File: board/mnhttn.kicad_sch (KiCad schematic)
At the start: 10 parts, among them SW1 SW_Push, SW2 SW_SPDT, SW3 SW_Push, SW4 SW_SPDT, U1 xiao-ble, U2 xiao-ble

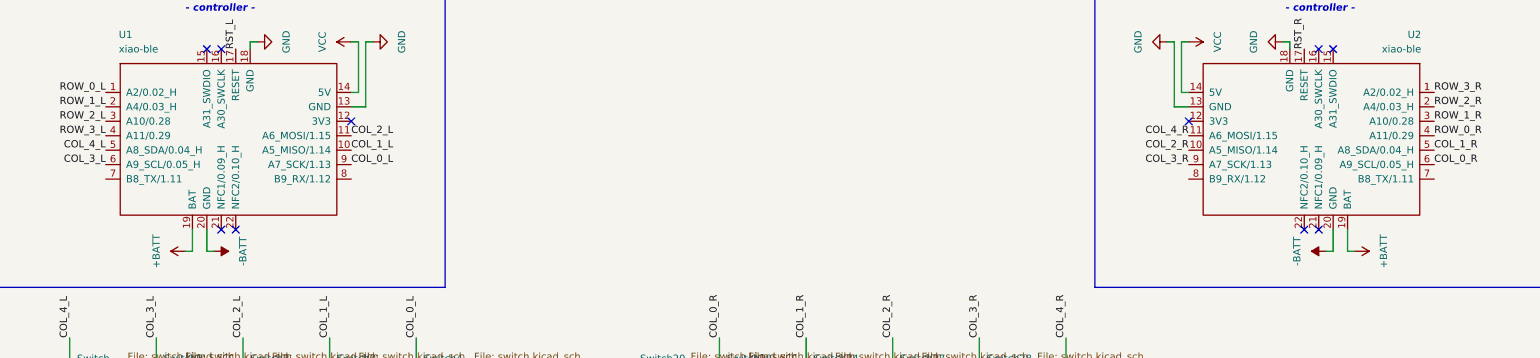
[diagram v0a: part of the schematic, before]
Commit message: Switched to SMD switches
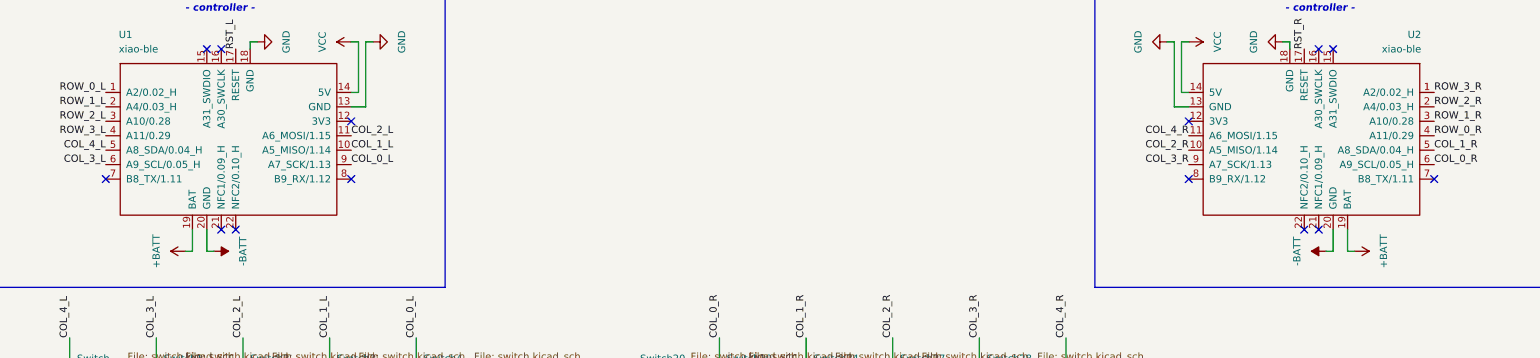
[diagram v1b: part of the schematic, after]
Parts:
- SW2, SW4: LCSC (none) -> C431541
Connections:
- no-connect marks 12 -> 16

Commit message: Add battery connector
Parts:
- removed BAT+1, BAT+2: +, mnhttn:BatteryPad, symbol Mechanical:MountingHole_Pad
- removed BAT-1, BAT-2: -, mnhttn:BatteryPad, symbol Mechanical:MountingHole_Pad
- added BT1, BT2: Battery_Cell, mnhttn:WAGO_2060-452_998-404, symbol Device:Battery_Cell
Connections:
- net -BATT: now also BT1.2 (-), BT2.2 (-)
- net at SW4.3 (C): now also BT2.1 (+)
- net at SW2.2 (B): now also BT1.1 (+)
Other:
- moved on the sheet: SW2, SW4

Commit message: SMD only, On/Off symbole, Cleanup
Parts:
- BT1, BT2: Digikey (none) -> 2946-2060-472/998-404TR-ND
- SW1, SW3: Digikey (none) -> EG5470TR-ND
- SW2, SW4: Digikey (none) -> 732-13665-2-ND; LCSC C431541 -> (none)
- U1, U2: footprint mnhttn:xiao-ble-smd-cutout -> mnhttn:xiao-ble-smd; Digikey (none) -> 1597-102010448-ND
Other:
- sheet Switch ports: added none; removed DIN, DOUT
- sheet Switch1 ports: added none; removed DIN, DOUT
- sheet Switch10 ports: added none; removed DIN, DOUT
- sheet Switch11 ports: added none; removed DIN, DOUT
- sheet Switch12 ports: added none; removed DIN, DOUT
- sheet Switch13 ports: added none; removed DIN, DOUT
- sheet Switch14 ports: added none; removed DIN, DOUT
- sheet Switch15 ports: added none; removed DIN, DOUT
- sheet Switch16 ports: added none; removed DIN, DOUT
- sheet Switch17 ports: added none; removed DIN, DOUT
- sheet Switch18 ports: added none; removed DIN, DOUT
- sheet Switch19 ports: added none; removed DIN, DOUT
- sheet Switch2 ports: added none; removed DIN, DOUT
- sheet Switch20 ports: added none; removed DIN, DOUT
- sheet Switch21 ports: added none; removed DIN, DOUT
- sheet Switch22 ports: added none; removed DIN, DOUT
- sheet Switch23 ports: added none; removed DIN, DOUT
- sheet Switch24 ports: added none; removed DIN, DOUT
- sheet Switch25 ports: added none; removed DIN, DOUT
- sheet Switch26 ports: added none; removed DIN, DOUT
- sheet Switch27 ports: added none; removed DIN, DOUT
- sheet Switch28 ports: added none; removed DIN, DOUT
- sheet Switch29 ports: added none; removed DIN, DOUT
- sheet Switch3 ports: added none; removed DIN, DOUT
- sheet Switch30 ports: added none; removed DIN, DOUT
- sheet Switch31 ports: added none; removed DIN, DOUT
- sheet Switch32 ports: added none; removed DIN, DOUT
- sheet Switch33 ports: added none; removed DIN, DOUT
- sheet Switch34 ports: added none; removed DIN, DOUT
- sheet Switch35 ports: added none; removed DIN, DOUT
- sheet Switch4 ports: added none; removed DIN, DOUT
- sheet Switch5 ports: added none; removed DIN, DOUT
- sheet Switch6 ports: added none; removed DIN, DOUT
- sheet Switch7 ports: added none; removed DIN, DOUT
- sheet Switch8 ports: added none; removed DIN, DOUT
- sheet Switch9 ports: added none; removed DIN, DOUT
